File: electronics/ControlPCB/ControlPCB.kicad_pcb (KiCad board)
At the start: 2 copper layers, 40 parts, among them CON1 12VINPUT, P1 Opto1, P2 Opto2, P3 Opto3, P4 Opto4, P5 Opto5, P6 Opto6, P7 Tool, U1 POLOLU_A4988, U2 POLOLU_A4988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

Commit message: ControlPCB update
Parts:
- removed PI1: VCCINPUT, Pin_Headers:Pin_Header_Straight_1x02
- moved CON1 66.3 mm to (94.2, 115.3)
- moved P6 39.4 mm to (201.9, 71.6)
- moved C5 28.4 mm to (114.3, 115.3)
- moved C6 28.4 mm to (134.6, 115.3)
- moved C7 28.4 mm to (154.9, 115.3)
- moved U5 28.4 mm to (123.2, 115.6)
- moved U7 28.4 mm to (163.8, 115.6)
- moved PM5 28.4 mm to (119.4, 105.4)
- moved PM6 28.4 mm to (139.7, 105.4)
- moved R5 28.4 mm to (114.3, 125.0)
- moved R6 28.4 mm to (134.6, 125.0)
- moved R7 28.4 mm to (154.9, 125.0)
- moved U6 28.4 mm to (143.5, 115.6)
- moved PM7 28.1 mm to (160.0, 105.4)
- moved P2 28.0 mm to (201.9, 85.9)
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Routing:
- net VCC: track 129.6 -> 625.8 mm
- net +12V: track 24.4 -> 231.8 mm
- net ENABLEM5: track 0.00 -> 135.2 mm
- net STEPM5: track 0.00 -> 112.4 mm
- net DIRM5: track 0.00 -> 100.4 mm
- net ENABLEM6: track 0.00 -> 88.8 mm
- net STEPM6: track 0.00 -> 67.4 mm
- net DIRM6: track 0.00 -> 56.9 mm
- net ENABLEM7: track 0.00 -> 47.7 mm
- net STEPM7: track 0.00 -> 30.2 mm
- net DIRM7: track 0.00 -> 26.0 mm
- net STOOL: track 0.00 -> 10.2 mm
- net SOPTO1: track 0.00 -> 10.2 mm
- net SOPTO2: track 0.00 -> 9.73 mm
- net SOPTO6: track 0.00 -> 9.73 mm
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- added copper zone on B.Cu, net GND

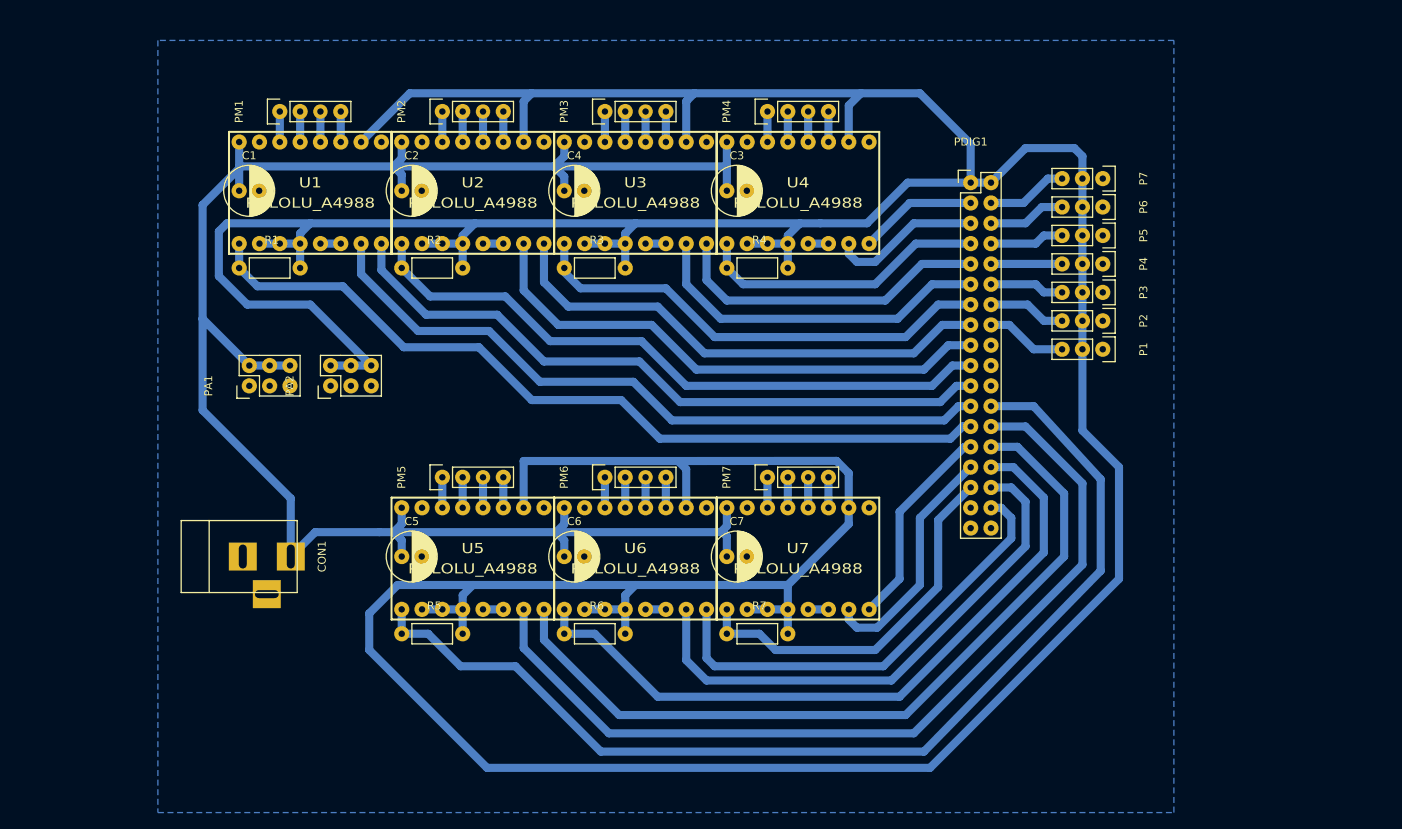
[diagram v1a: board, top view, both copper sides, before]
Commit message: ControlPCB updated, gerber and drills files added
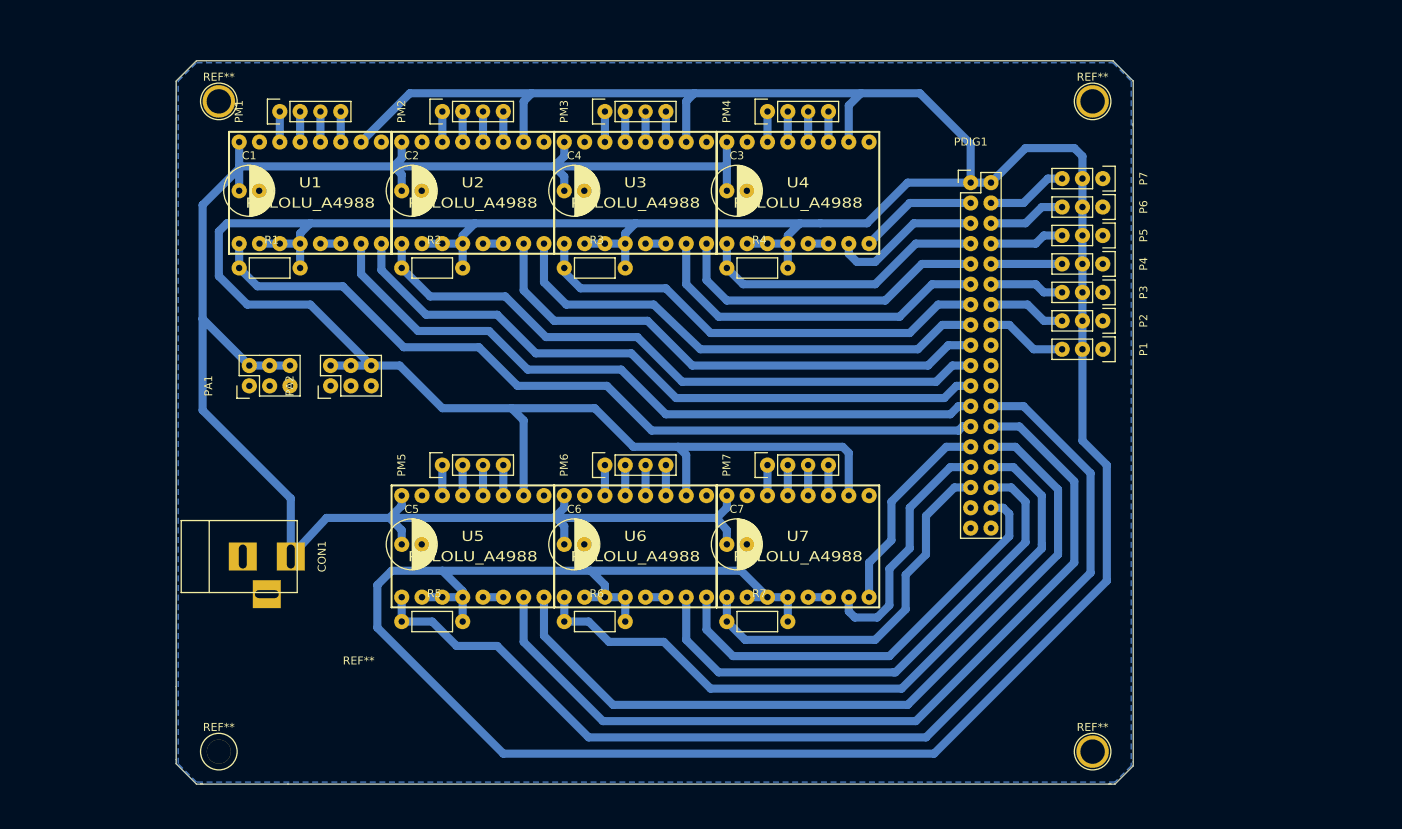
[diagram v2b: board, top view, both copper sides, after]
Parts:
- added REF**: Symbol_OSHW-Logo_CopperTop_BIG, Symbols:Symbol_OSHW-Logo_CopperTop_BIG, F.Cu at (109.2, 116.8)
- added REF**: 1pin, Connect:1pin, F.Cu at (91.4, 139.7)
- added REF**: 1pin, Connect:1pin, F.Cu at (91.4, 58.4)
- added REF**: 1pin, Connect:1pin, F.Cu at (200.7, 139.7)
- added REF**: 1pin, Connect:1pin, F.Cu at (200.7, 58.4)
- moved C5 1.52 mm to (114.3, 113.8)
- moved C6 1.52 mm to (134.6, 113.8)
- moved C7 1.52 mm to (154.9, 113.8)
- moved PM5 1.52 mm to (119.4, 103.9)
- moved PM6 1.52 mm to (139.7, 103.9)
- moved PM7 1.52 mm to (160.0, 103.9)
- moved R5 1.52 mm to (114.3, 123.4)
- moved R6 1.52 mm to (134.6, 123.4)
- moved R7 1.52 mm to (154.9, 123.4)
- moved U5 1.52 mm to (123.2, 114.0)
- moved U6 1.52 mm to (143.5, 114.0)
- moved U7 1.52 mm to (163.8, 114.0)
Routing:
- net VCC: track 625.8 -> 635.6 mm
- net ENABLEM5: track 135.2 -> 132.0 mm
- net STEPM5: track 112.4 -> 110.1 mm
- net DIRM6: track 56.9 -> 54.9 mm
- net DIRM5: track 100.4 -> 99.2 mm
- net STEPM6: track 67.4 -> 66.3 mm
- net +12V: track 231.8 -> 232.8 mm
- net ENABLEM6: track 88.8 -> 87.9 mm
- net ENABLEM1: track 104.0 -> 103.1 mm
- net STEPM1: track 88.3 -> 87.7 mm
- net STEPM7: track 30.2 -> 30.8 mm
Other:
- board outline added: 119.6 x 90.4 mm
